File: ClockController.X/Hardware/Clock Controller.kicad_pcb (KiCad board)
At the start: 2 copper layers, 63.5 x 44.5 mm, 47 parts, among them J1 UJC-VP-3-SMT-TR, J2 HDR-1X2H, Q1 DMG7430LFG-7, Q2 FDD7N25LZTM, Q3 MMBT2222A-TP, Q4 MMBT2907ALT1G, Q5 MMBT2222A-TP, Q6 MMBT2222A-TP, U1 PIC16F15224-I/SL, U2 AS78L05RTR-E1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

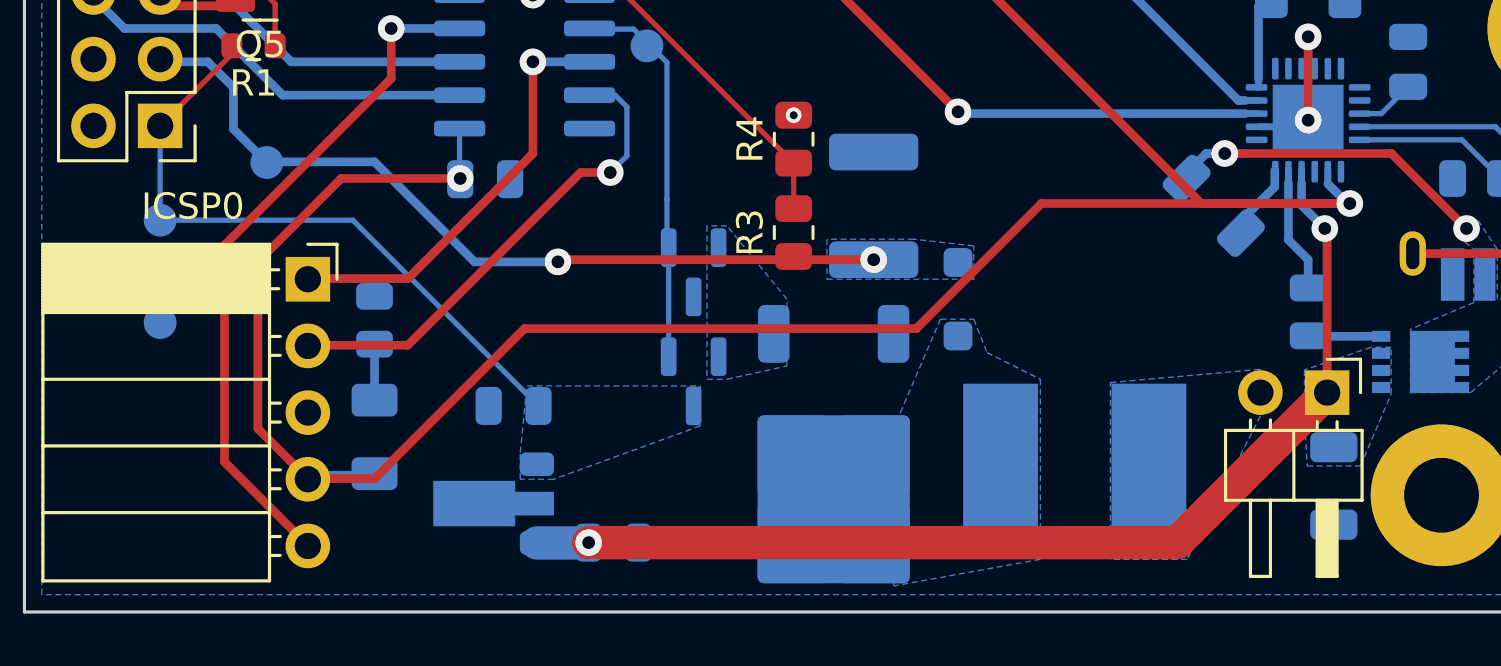
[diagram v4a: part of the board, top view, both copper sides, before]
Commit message: Moved the VRM closer to the main load
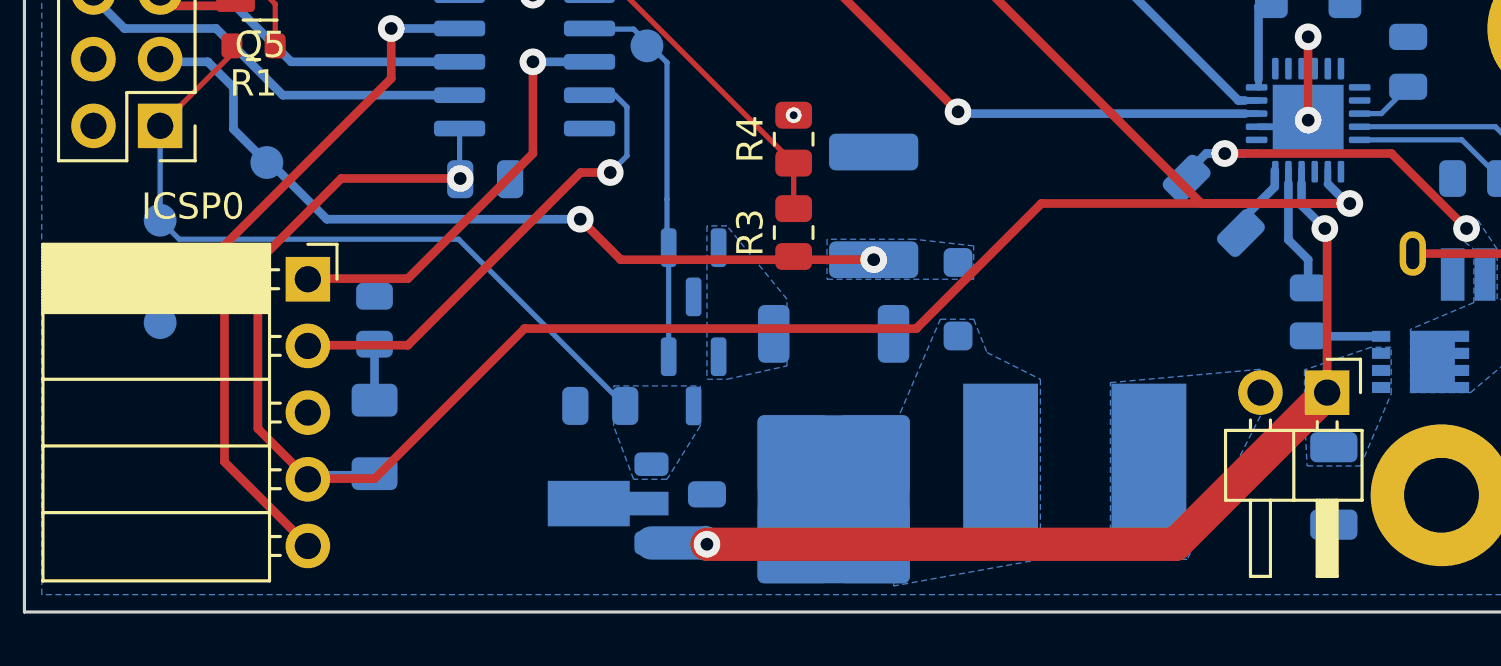
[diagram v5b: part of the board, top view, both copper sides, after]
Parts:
- moved U2 4.36 mm to (138.7, 123.1)
- moved C6 3.67 mm to (142.7, 123.7), turned to -89.999 degrees
- moved C5 3.30 mm to (138.7, 119.4)
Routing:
- net +20V: track 41.4 -> 37.0 mm
- net +5V: track 25.1 -> 28.4 mm
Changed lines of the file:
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@@
 	(footprint "Package_TO_SOT_SMD:SOT-89-3"
 		(layer "B.Cu")
-		(at 134.32 123.1005 180)
+		(at 138.684 123.1005 180)
 		(descr "SOT-89-3, http://ww1.microchip.com/downloads/en/DeviceDoc/3L_SOT-89_MB_C04-029C.pdf")
 		(tags "SOT-89-3")
 		(property "Reference" "U2"
-			(at -3.856 1.4345 0)
+			(at 3.302 -0.0895 0)
 			(layer "B.SilkS")
 			(effects
@@
 		(tags "SOT TO_SOT_SMD")
 		(property "Reference" "Q3"
-			(at 0.15234 2.832103 0.001262754521)
+			(at -1.094567 3.047955 0.001262754521)
 			(layer "B.SilkS")
 			(effects
@@
 	(footprint "Capacitor_SMD:C_0805_2012Metric"
 		(layer "B.Cu")
-		(at 139.192 124.587 -179.999)
+		(at 142.748 123.698 -89.999)
 		(descr "Capacitor SMD 0805 (2012 Metric), square (rectangular) end terminal, IPC_7351 nominal, (Body size source: IPC-SM-782 page 76, https://www.pcb-3d.com/wordpress/wp-content/uploads/ipc-sm-782a_amendment_1_and_2.pdf, https://docs.google.com/spreadsheets/d/1BsfQQcO9C6DZCsRaXUlFlo91Tg2WpOkGARC1WS5S8t0/edit?usp=sharing), generated with kicad-footprint-generator")
 		(tags "capacitor")
 		(property "Reference" "C6"
-			(at -2.895599 -0.03816 0.001)
+			(at -2.285999 -0.038149 180.001)
 			(layer "B.SilkS")
 			(effects
@@
 		)
 		(property "Value" "100nF"
-			(at 0 -1.68 0.001)
+			(at 0 -1.68 90.001)
 			(layer "B.Fab")
 			(hide yes)
@@
 		)
 		(property "Datasheet" ""
-			(at 0 0 0.001)
+			(at 0 0 90.001)
 			(unlocked yes)
 			(layer "B.Fab")
@@
 		)
 		(property "Description" ""
-			(at 0 0 0.001)
+			(at 0 0 90.001)
 			(unlocked yes)
 			(layer "B.Fab")
@@
 		)
 		(fp_line
-			(start 1.700001 0.980001)
-			(end -1.699999 0.979999)
+			(start -1.699999 0.979999)
+			(end -1.700001 -0.980001)
 			(stroke
 				(width 0.05)
@@
 		)
 		(fp_line
-			(start 1.699999 -0.979999)
-			(end 1.700001 0.980001)
+			(start 1.700001 0.980001)
+			(end -1.699999 0.979999)
 			(stroke
 				(width 0.05)
@@
 		)
 		(fp_line
-			(start -1.699999 0.979999)
-			(end -1.700001 -0.980001)
+			(start -1.700001 -0.980001)
+			(end 1.699999 -0.979999)
 			(stroke
 				(width 0.05)
@@
 		)
 		(fp_line
-			(start -1.700001 -0.980001)
-			(end 1.699999 -0.979999)
+			(start 1.699999 -0.979999)
+			(end 1.700001 0.980001)
 			(stroke
 				(width 0.05)
@@
 		)
 		(fp_line
-			(start 1 0.625)
-			(end -1 0.625)
+			(start -1 0.625)
+			(end -1 -0.625)
 			(stroke
 				(width 0.1)
@@
 		)
 		(fp_line
-			(start 1 -0.625)
-			(end 1 0.625)
+			(start 1 0.625)
+			(end -1 0.625)
 			(stroke
 				(width 0.1)
@@
 		)
 		(fp_line
-			(start -1 0.625)
-			(end -1 -0.625)
+			(start -1 -0.625)
+			(end 1 -0.625)
 			(stroke
 				(width 0.1)
@@
 		)
 		(fp_line
-			(start -1 -0.625)
-			(end 1 -0.625)
+			(start 1 -0.625)
+			(end 1 0.625)
 			(stroke
 				(width 0.1)
@@
 		)
 		(fp_text user "${REFERENCE}"
-			(at 0 0 0.001)
+			(at 0 0 90.001)
 			(layer "B.Fab")
 			(effects
@@
 		)
 		(pad "1" smd roundrect
-			(at -0.95 0 180.001)
+			(at -0.95 0 270.001)
 			(size 1 1.45)
 			(layers "B.Cu" "B.Mask" "B.Paste")
@@
 		)
 		(pad "2" smd roundrect
-			(at 0.95 0 180.001)
+			(at 0.95 0 270.001)
 			(size 1 1.45)
 			(layers "B.Cu" "B.Mask" "B.Paste")
@@
 	(footprint "Capacitor_SMD:C_0805_2012Metric"
 		(layer "B.Cu")
-		(at 135.382 119.38 0.002104591424)
+		(at 138.684 119.38 0.002104591424)
 		(descr "Capacitor SMD 0805 (2012 Metric), square (rectangular) end terminal, IPC_7351 nominal, (Body size source: IPC-SM-782 page 76, https://www.pcb-3d.com/wordpress/wp-content/uploads/ipc-sm-782a_amendment_1_and_2.pdf, https://docs.google.com/spreadsheets/d/1BsfQQcO9C6DZCsRaXUlFlo91Tg2WpOkGARC1WS5S8t0/edit?usp=sharing), generated with kicad-footprint-generator")
 		(tags "capacitor")
 		(property "Reference" "C5"
-			(at 0.000065 -1.778 180.0021046)
+			(at -2.794 -0.000103 180.0021046)
 			(layer "B.SilkS")
 			(effects
@@
 		(tags "SOT TO_SOT_SMD")
 		(property "Reference" "Q4"
-			(at 0.08884 2.832102 0.001262754521)
+			(at -1.005665 3.047957 0.001262754521)
 			(layer "B.SilkS")
 			(effects
@@
 	)
 	(segment
-		(start 160.654983 124.587017)
-		(end 138.242 124.587017)
+		(start 160.594 124.648)
+		(end 166.37 118.872)
 		(width 1.27)
 		(layer "F.Cu")
@@
 	)
 	(segment
-		(start 166.37 118.872)
-		(end 160.654983 124.587017)
-		(width 1.27)
+		(start 166.2811 112.6236)
+		(end 166.37 112.7125)
+		(width 0.33)
 		(layer "F.Cu")
 		(net 1)
 	)
 	(segment
-		(start 166.2811 112.6236)
-		(end 166.37 112.7125)
-		(width 0.33)
+		(start 142.748017 124.648)
+		(end 160.594 124.648)
+		(width 1.27)
 		(layer "F.Cu")
 		(net 1)
@@
 	)
 	(via
-		(at 138.242 124.587017)
+		(at 142.748017 124.648)
 		(size 1.016)
 		(drill 0.485667)
@@
 	)
 	(segment
-		(start 138.228517 124.6005)
-		(end 138.242 124.587017)
+		(start 142.700517 124.6005)
+		(end 142.748017 124.648)
 		(width 1.27)
 		(layer "B.Cu")
@@
 	)
 	(segment
-		(start 136.27 124.6005)
-		(end 138.228517 124.6005)
+		(start 140.634 124.6005)
+		(end 142.700517 124.6005)
 		(width 1.27)
 		(layer "B.Cu")
@@
 	)
 	(segment
+		(start 122.6439 113.03)
+		(end 121.92 112.3061)
+		(width 0.2)
+		(layer "B.Cu")
+		(net 2)
+	)
+	(segment
 		(start 121.92 112.3061)
 		(end 121.92 108.712)
@@
 	)
 	(segment
-		(start 129.258135 112.3061)
-		(end 121.92 112.3061)
+		(start 133.284035 113.03)
+		(end 122.6439 113.03)
 		(width 0.2)
 		(layer "B.Cu")
@@
 	)
 	(segment
-		(start 136.332 119.379965)
-		(end 129.258135 112.3061)
+		(start 139.634 119.379965)
+		(end 133.284035 113.03)
 		(width 0.2)
 		(layer "B.Cu")
@@
 	)
 	(segment
-		(start 137.1547 113.81)
-		(end 149.098173 113.81)
+		(start 137.922 112.268)
+		(end 139.464 113.81)
 		(width 0.33)
 		(layer "F.Cu")
@@
 	)
 	(segment
-		(start 137.0711 113.8936)
-		(end 137.1547 113.81)
+		(start 139.464 113.81)
+		(end 149.098173 113.81)
 		(width 0.33)
 		(layer "F.Cu")
@@
 	)
 	(via
-		(at 137.0711 113.8936)
+		(at 137.922 112.268)
 		(size 1.016)
 		(drill 0.485667)
@@
 	)
 	(segment
-		(start 126.0094 110.0836)
-		(end 125.984 110.109)
+		(start 137.922 112.268)
+		(end 128.27 112.268)
 		(width 0.33)
 		(layer "B.Cu")
@@
 	)
 	(segment
-		(start 124.714 108.839)
-		(end 125.984 110.109)
+		(start 128.27 112.268)
+		(end 126.0856 110.0836)
 		(width 0.33)
 		(layer "B.Cu")
@@
 	)
 	(segment
-		(start 121.8311 106.2736)
-		(end 123.7361 106.2736)
+		(start 126.0856 110.0836)
+		(end 126.0094 110.0836)
 		(width 0.33)
 		(layer "B.Cu")
@@
 	)
 	(segment
-		(start 124.714 107.2515)
-		(end 124.714 108.839)
+		(start 124.714 108.839)
+		(end 125.984 110.109)
 		(width 0.33)
 		(layer "B.Cu")
@@
 	)
 	(segment
-		(start 137.0711 113.8936)
-		(end 133.8961 113.8936)
+		(start 121.8311 106.2736)
+		(end 123.7361 106.2736)
 		(width 0.33)
 		(layer "B.Cu")
@@
 	)
 	(segment
-		(start 130.0861 110.0836)
-		(end 126.0094 110.0836)
+		(start 124.714 107.2515)
+		(end 124.714 108.839)
 		(width 0.33)
 		(layer "B.Cu")
@@
 	)
 	(segment
-		(start 123.7361 106.2736)
-		(end 124.714 107.2515)
+		(start 126.0094 110.0836)
+		(end 125.984 110.109)
 		(width 0.33)
 		(layer "B.Cu")
@@
 	)
 	(segment
-		(start 133.8961 113.8936)
-		(end 130.0861 110.0836)
+		(start 123.7361 106.2736)
+		(end 124.714 107.2515)
 		(width 0.33)
 		(layer "B.Cu")
@@
 		(polygon
 			(pts
-				(xy 135.89 118.618) (xy 142.494 118.618) (xy 142.494 120.142) (xy 136.906 122.174) (xy 135.636 122.174)
-				(xy 135.636 121.158)
+				(xy 139.192 118.618) (xy 142.494 118.618) (xy 142.494 120.142) (xy 141.224 122.174) (xy 139.954 122.174)
+				(xy 139.192 120.142)
 			)
 		)

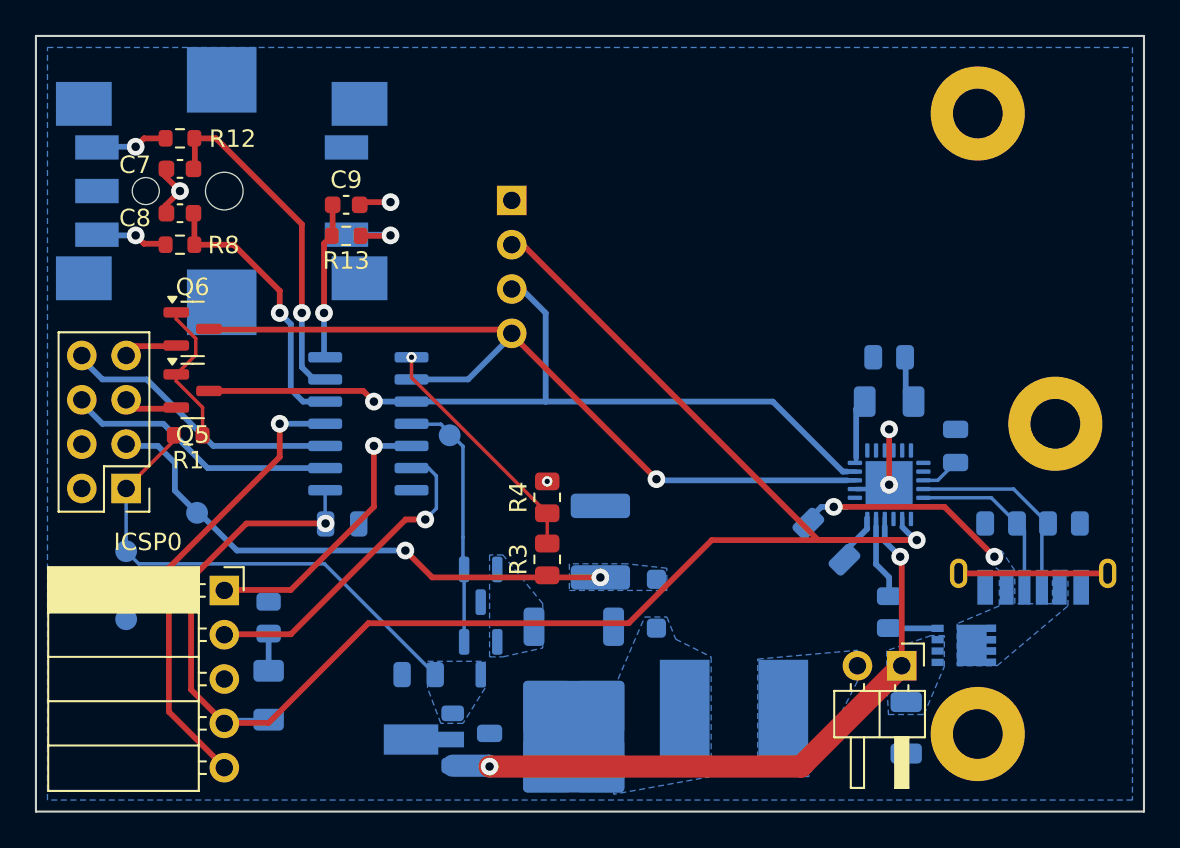
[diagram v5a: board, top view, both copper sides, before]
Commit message: Down-sized a bunch of resistor packags
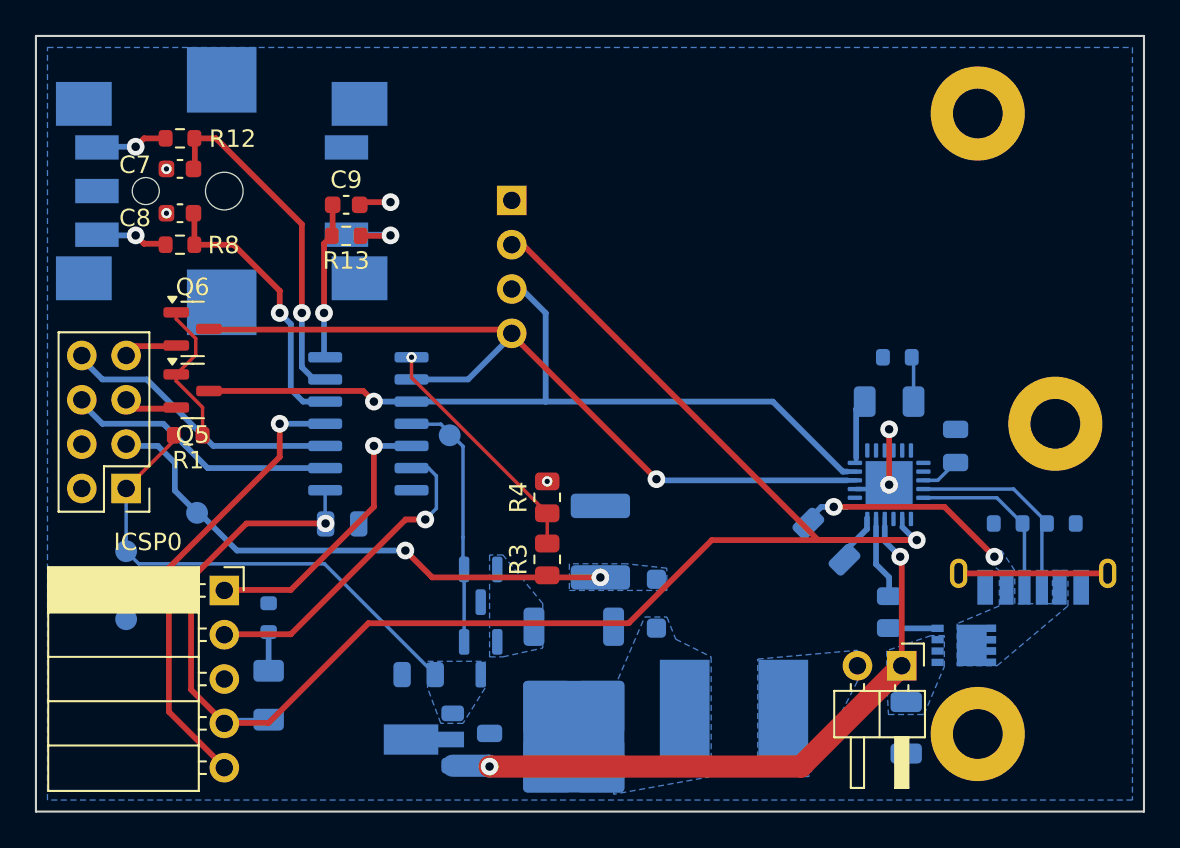
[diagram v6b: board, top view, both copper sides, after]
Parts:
- R10, R11, R5, R9: footprint Resistor_SMD:R_0805_2012Metric -> Resistor_SMD:R_0603_1608Metric
- moved R5 0.47 mm to (166.1, 101.2)
- moved R11 0.40 mm to (172.5, 110.7)
- moved R10 0.15 mm to (175.5, 110.7)
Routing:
- net GND: track 18.9 -> 15.7 mm, vias 5 -> 6

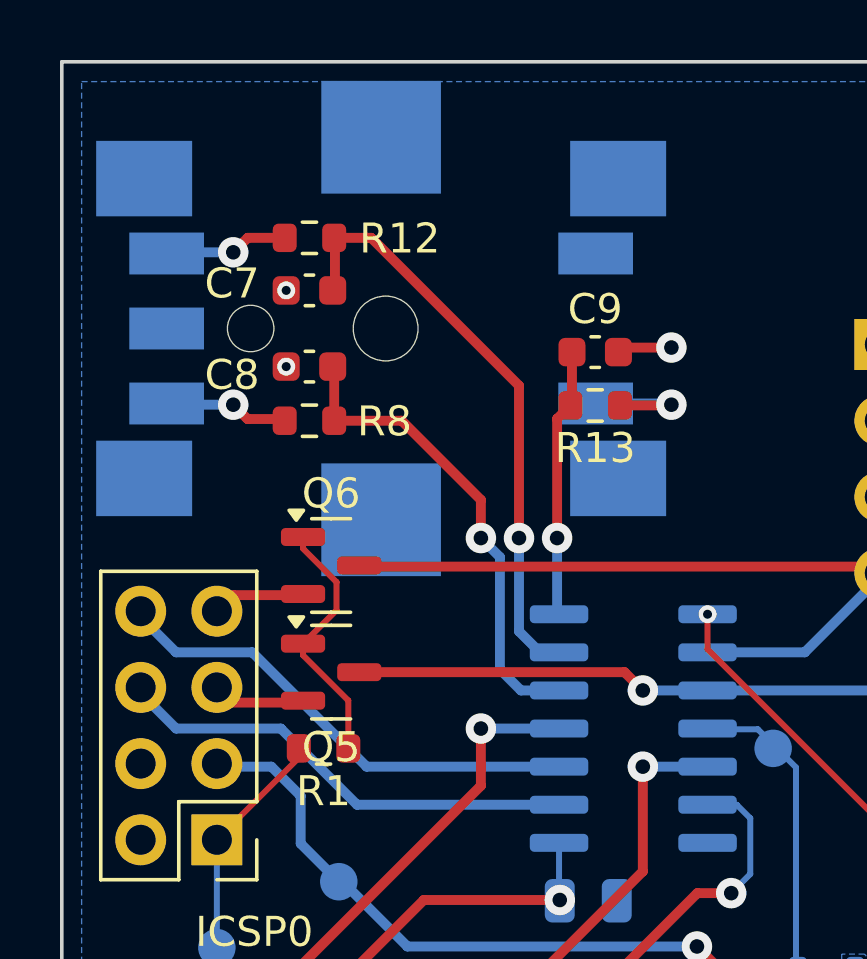
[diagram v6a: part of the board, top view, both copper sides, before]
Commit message: Cleanup of the silkscreens.
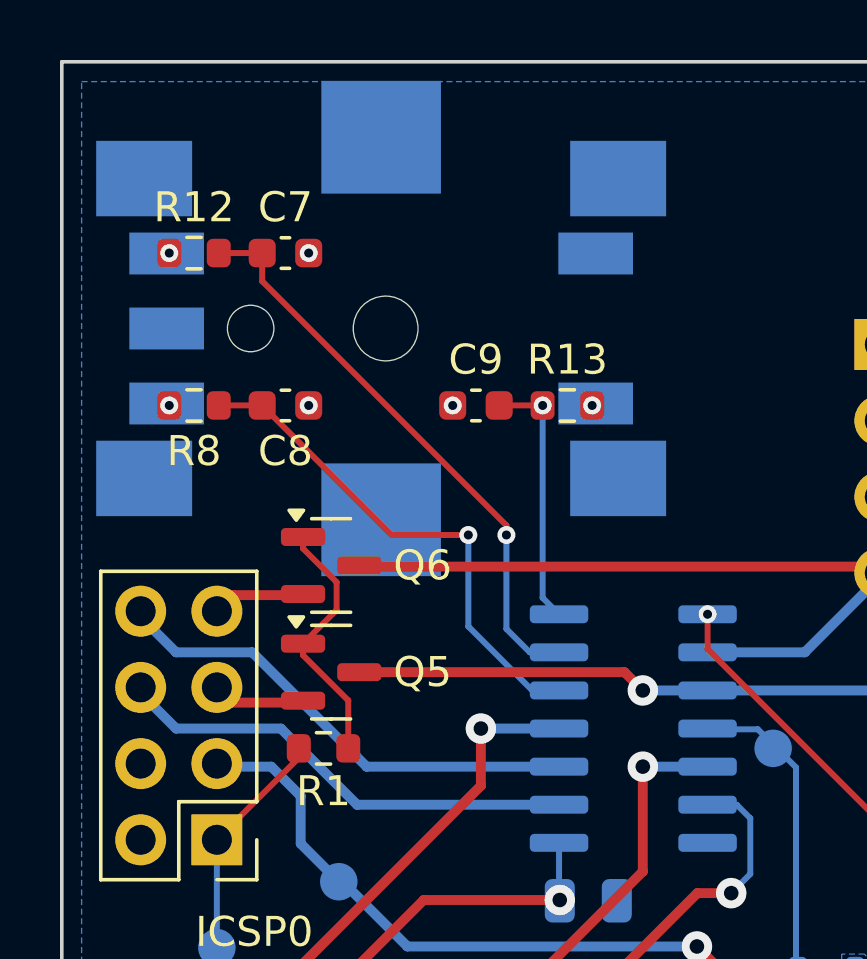
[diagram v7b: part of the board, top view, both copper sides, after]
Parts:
- moved C9 4.35 mm to (130.6, 94.2), turned to 180 degrees
- moved R8 3.88 mm to (121.2, 94.2)
- moved R12 3.88 mm to (121.2, 89.2)
- moved C8 1.52 mm to (124.2, 94.2), turned to 180 degrees
- moved C7 1.48 mm to (124.2, 89.2), turned to 0 degrees
- moved R13 0.93 mm to (133.6, 94.2)
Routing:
- net Net-(S1-D): track 4.27 -> 0.00 mm
- net Net-(S1-A): track 4.17 -> 0.00 mm
- net Net-(S1-B): track 4.15 -> 0.00 mm
- net GND: track 15.7 -> 13.9 mm
- net Rotary_A: track 16.0 -> 17.1 mm
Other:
- board text added: "Nixie Clock Controller (v1.1) Aaron Johnson 4/4/2026"
- board text removed: "Nixie Clock Controller Aaron Johnson 6/25/2024"
